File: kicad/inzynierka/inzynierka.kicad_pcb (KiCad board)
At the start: 2 copper layers, 170 x 175 mm, 36 parts

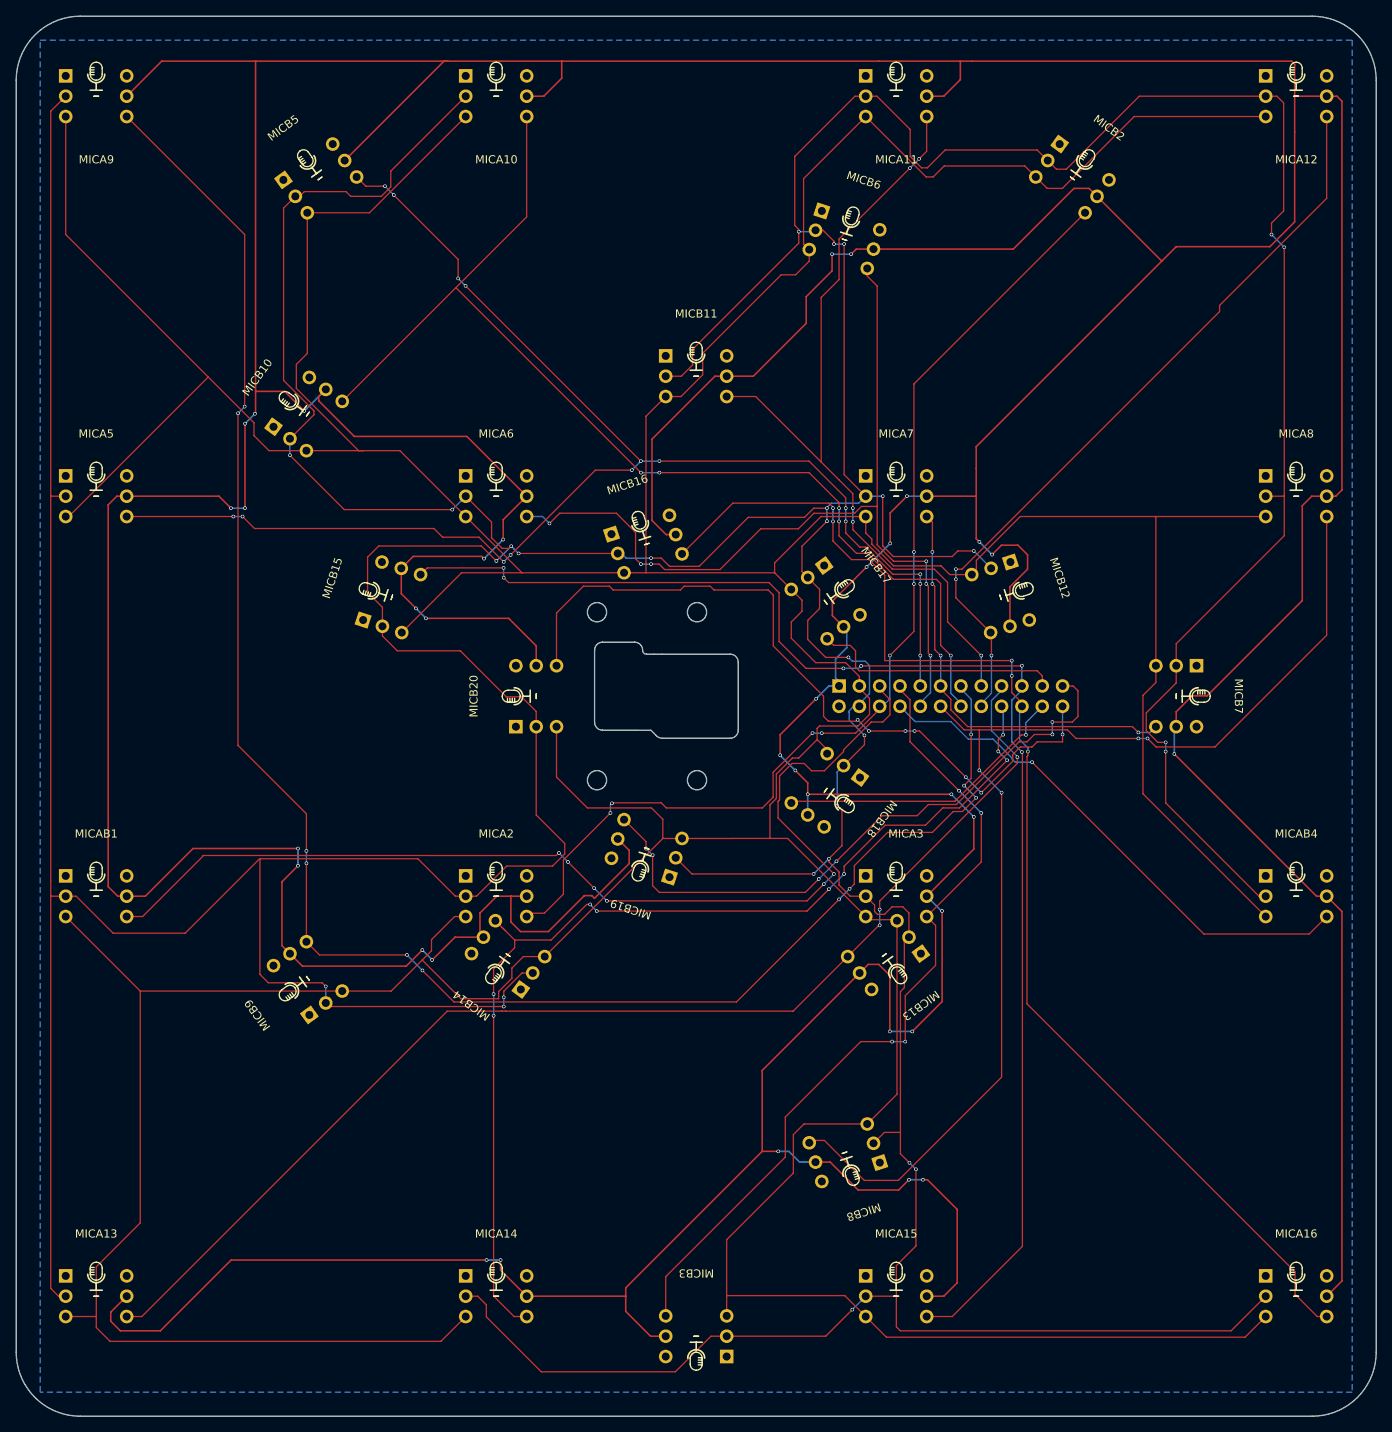
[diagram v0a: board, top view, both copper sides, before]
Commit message: Dodanie dziur montażowych
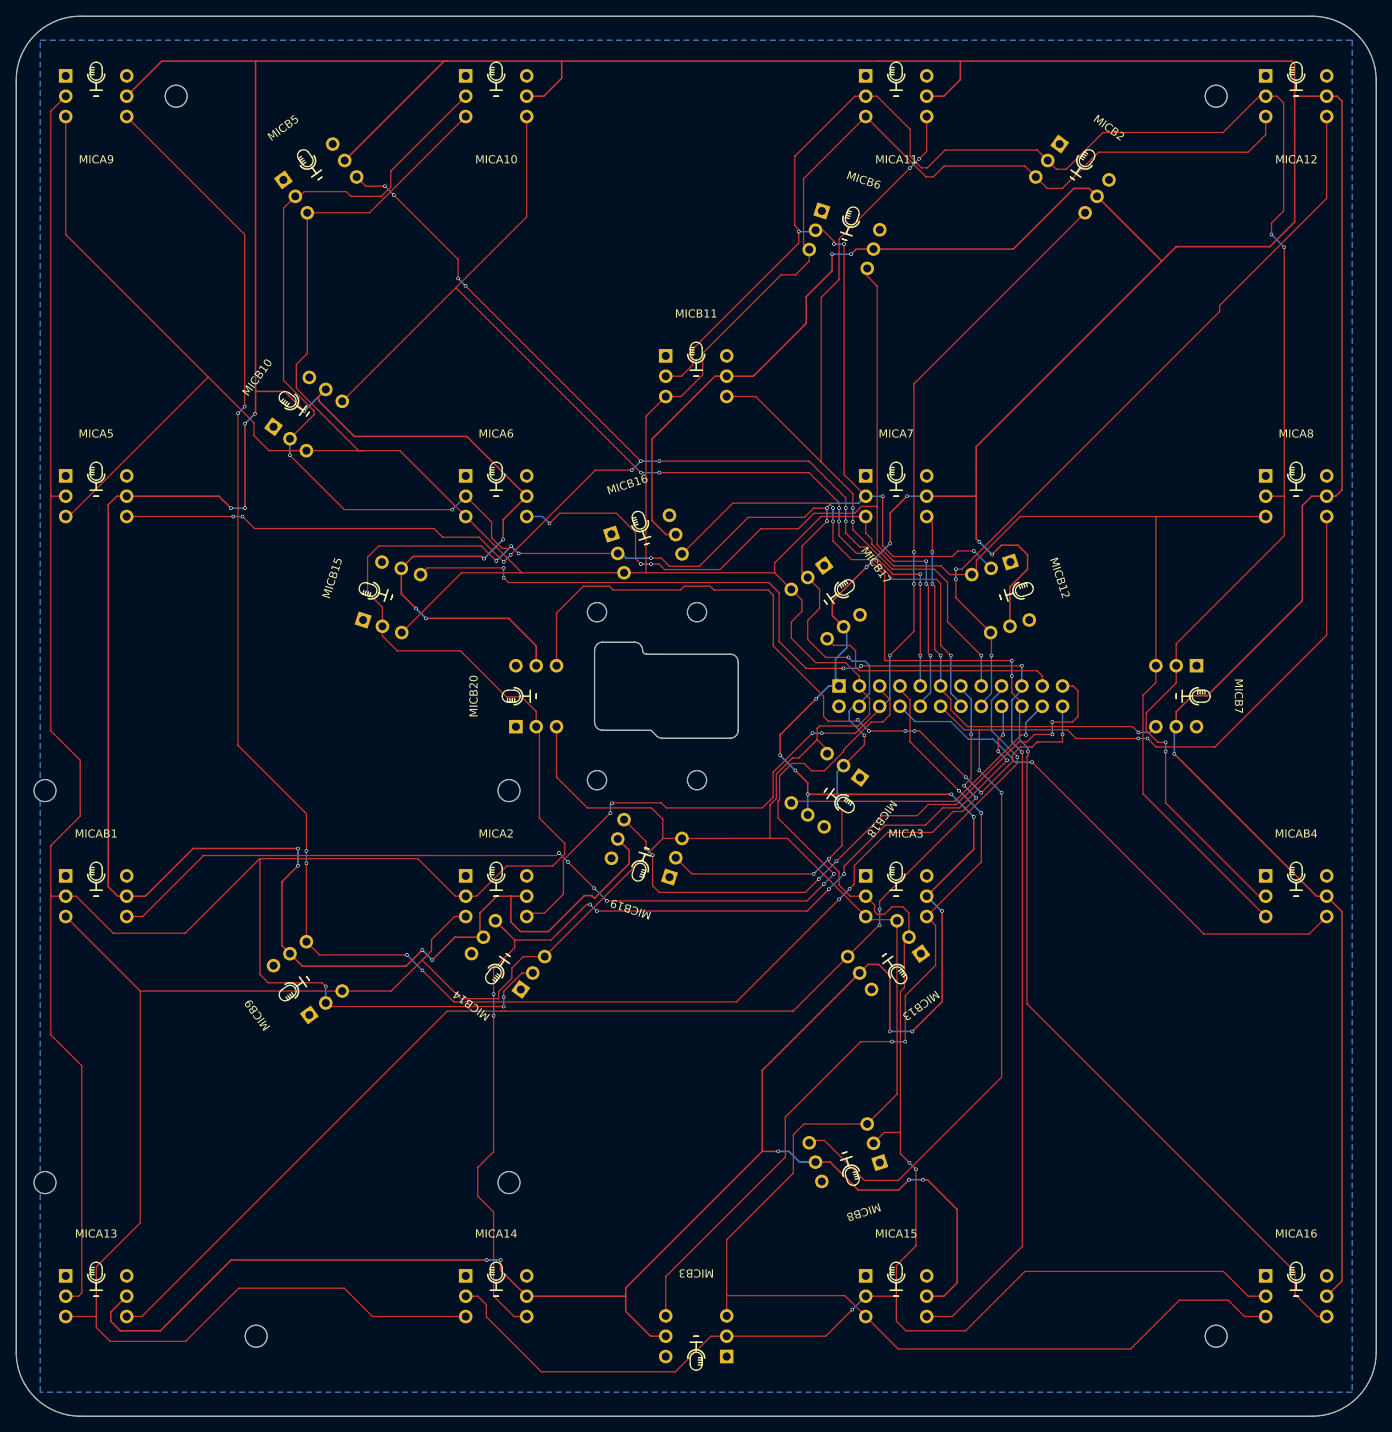
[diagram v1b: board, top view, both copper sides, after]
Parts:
- added ?: , , F.Cu at (46.5, 180.0)
- added ?: , , F.Cu at (166.5, 180.0)
- added ?: , , F.Cu at (166.5, 25.0)
- added ?: , , F.Cu at (36.5, 25.0)
- added REF**: RPI 3B, Moje:RPI 3B, B.Cu at (39.1, 136.3)
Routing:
- net CLK2: track 1057.2 -> 1064.5 mm
- net CLK1: track 923.9 -> 931.1 mm
- net D14: track 134.4 -> 136.1 mm

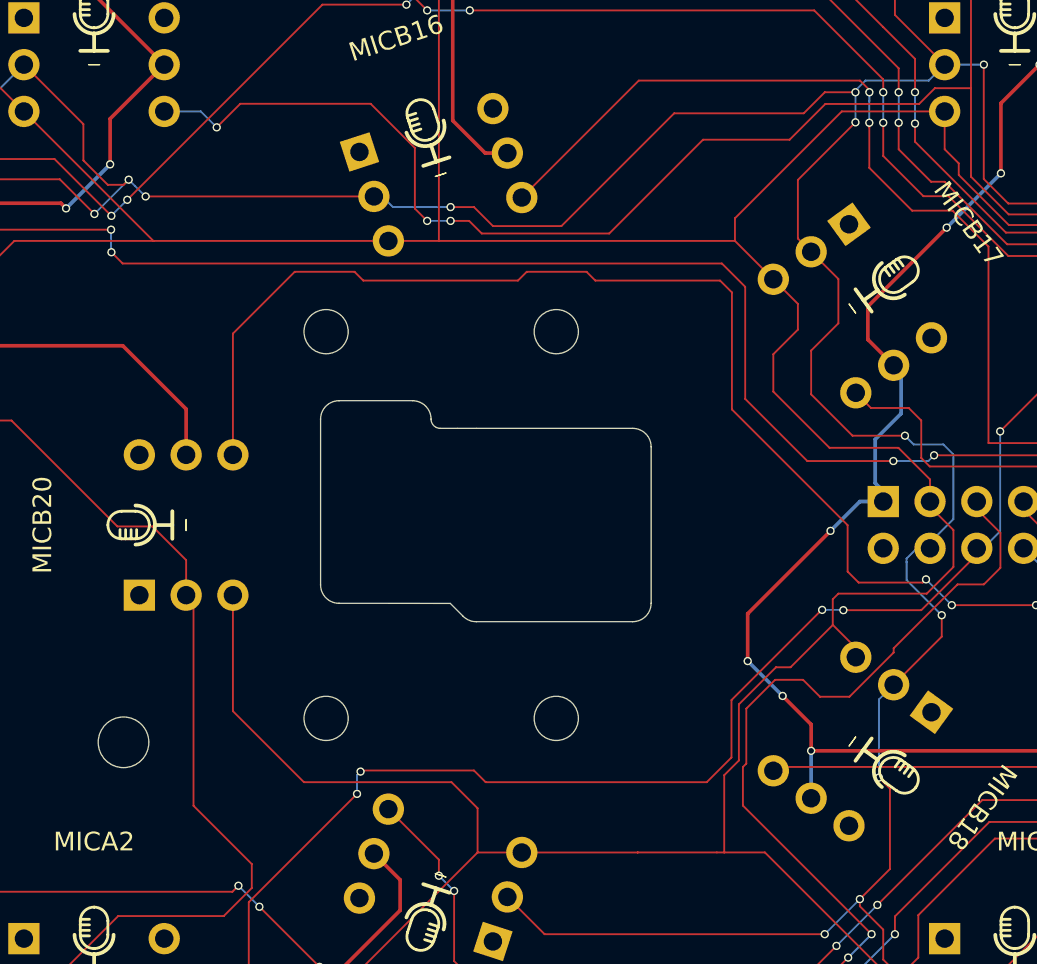
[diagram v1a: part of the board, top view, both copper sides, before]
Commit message: Poprawienie footprintu i odwrócenie kamery
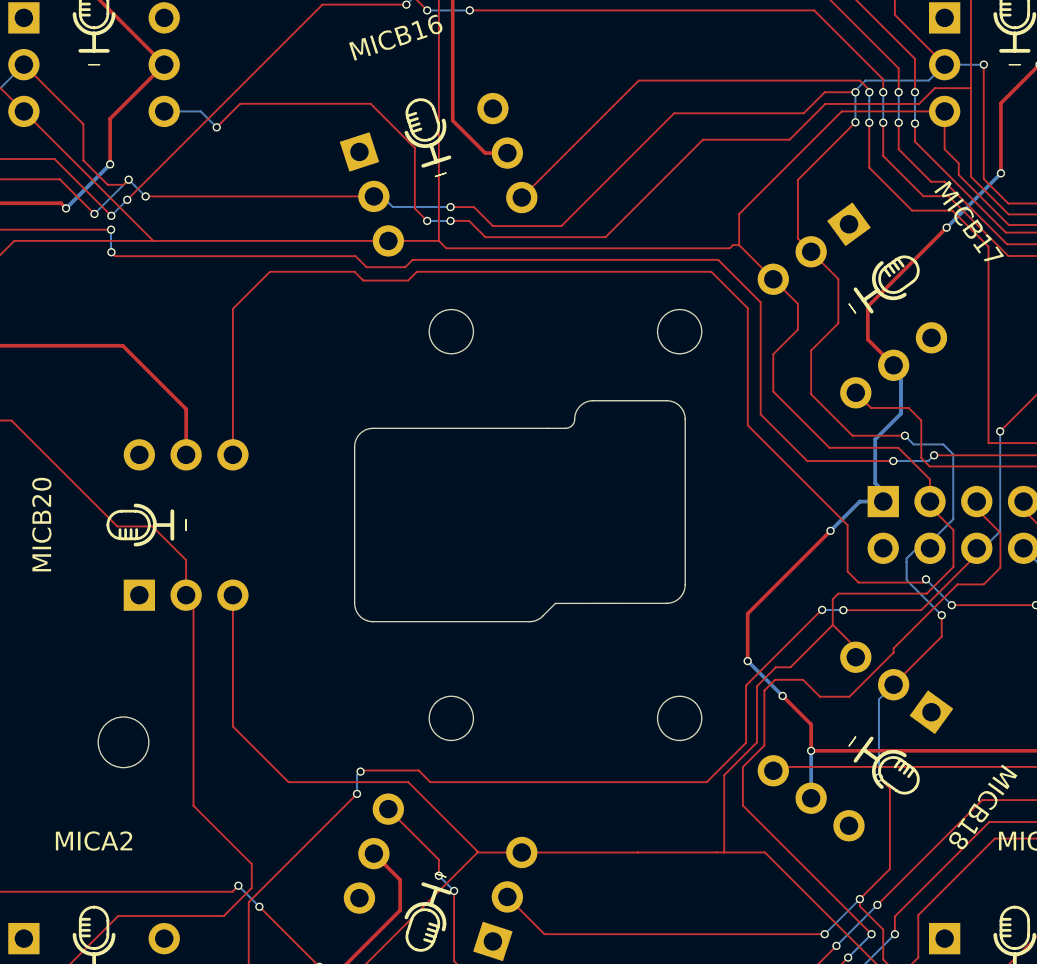
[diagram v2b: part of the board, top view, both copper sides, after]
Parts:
- moved REF** 5.60 mm to (95.9, 100.0), turned to -90 degrees
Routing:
- net D20: track 95.2 -> 96.0 mm
- net CLK1: track 931.1 -> 930.5 mm

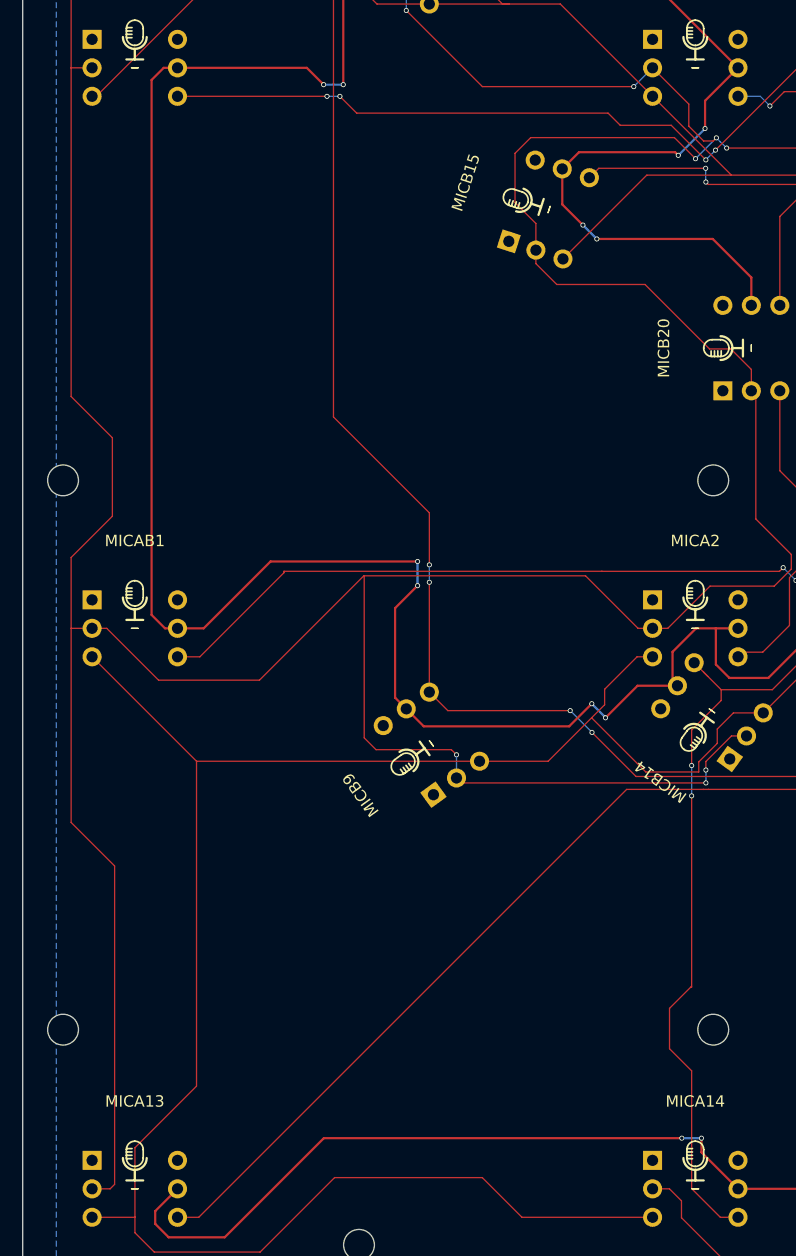
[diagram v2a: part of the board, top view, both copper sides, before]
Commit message: Przesunięto dziury montażowe dla RPI 3
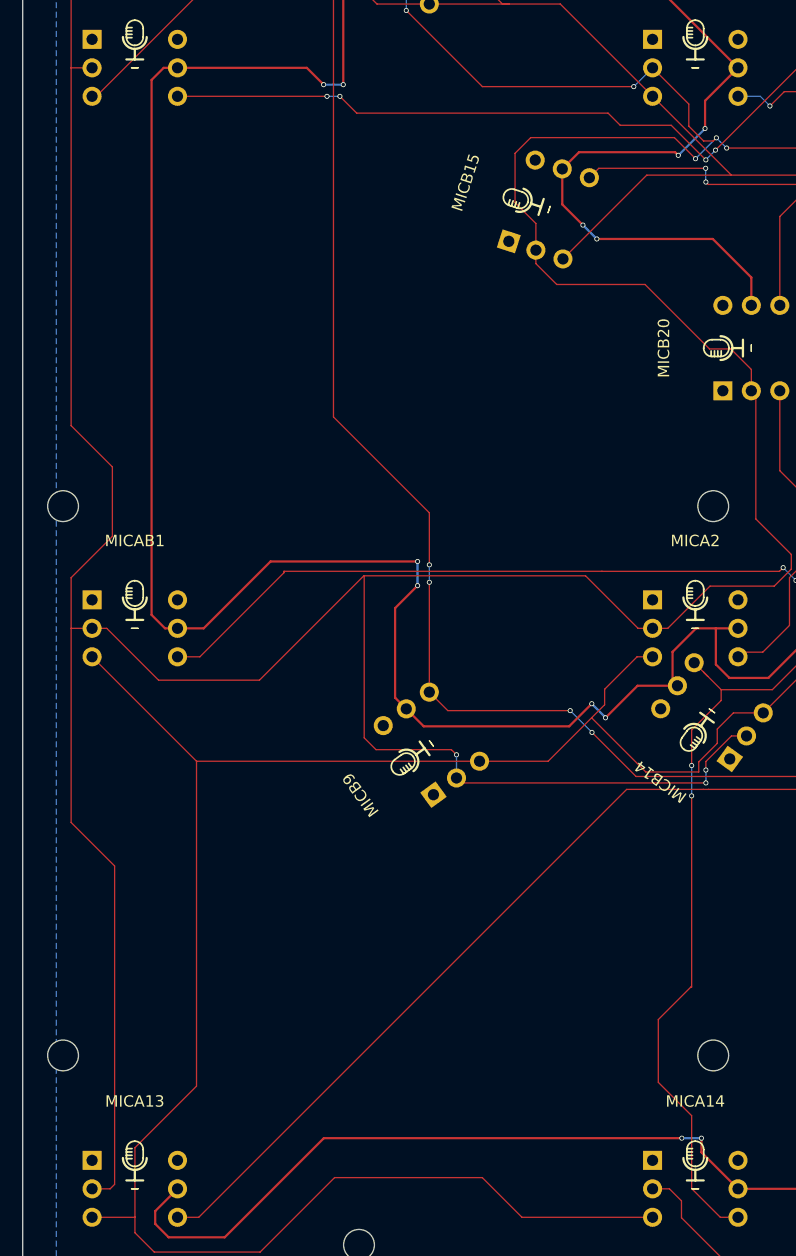
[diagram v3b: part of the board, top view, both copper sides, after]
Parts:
- moved REF** 2.30 mm to (39.1, 138.6)
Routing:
- net D14: track 136.1 -> 136.9 mm

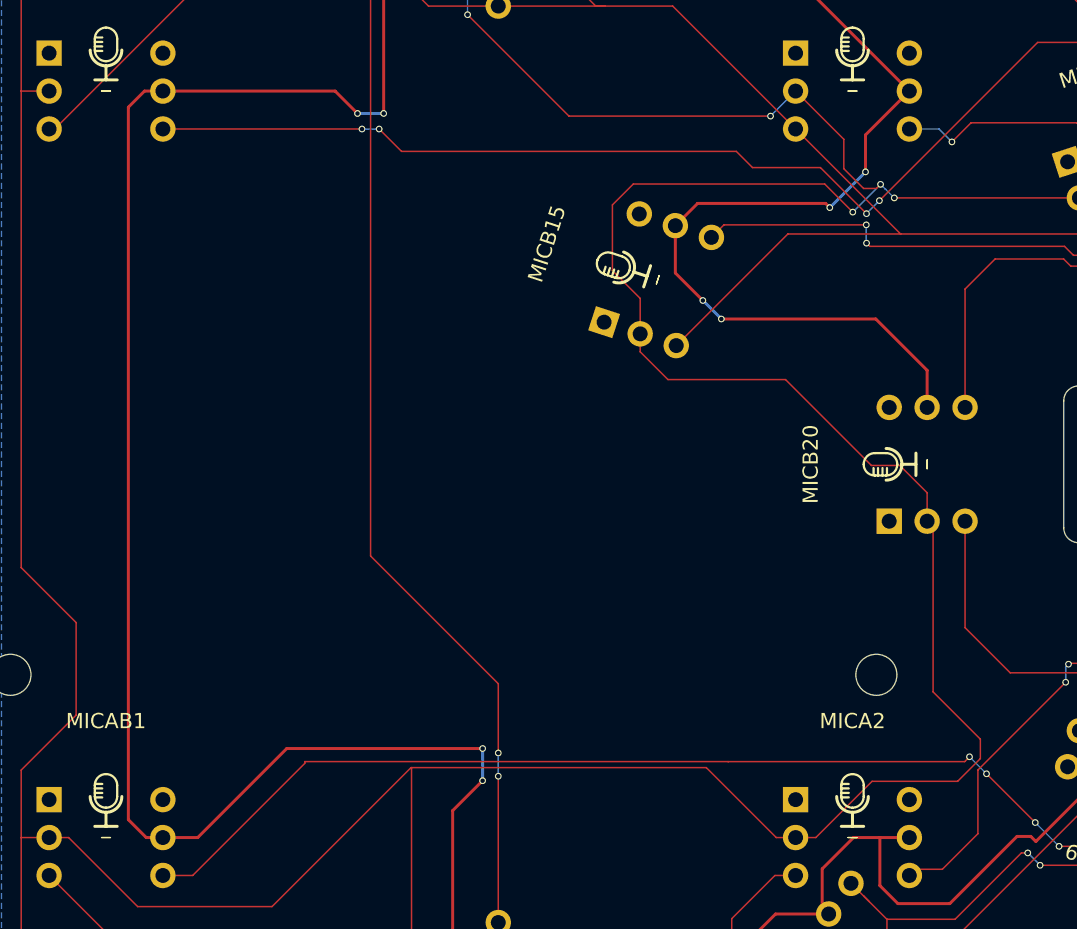
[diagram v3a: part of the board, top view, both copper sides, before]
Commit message: Rozpoczęcie dodawania opisów z tyłu płytki
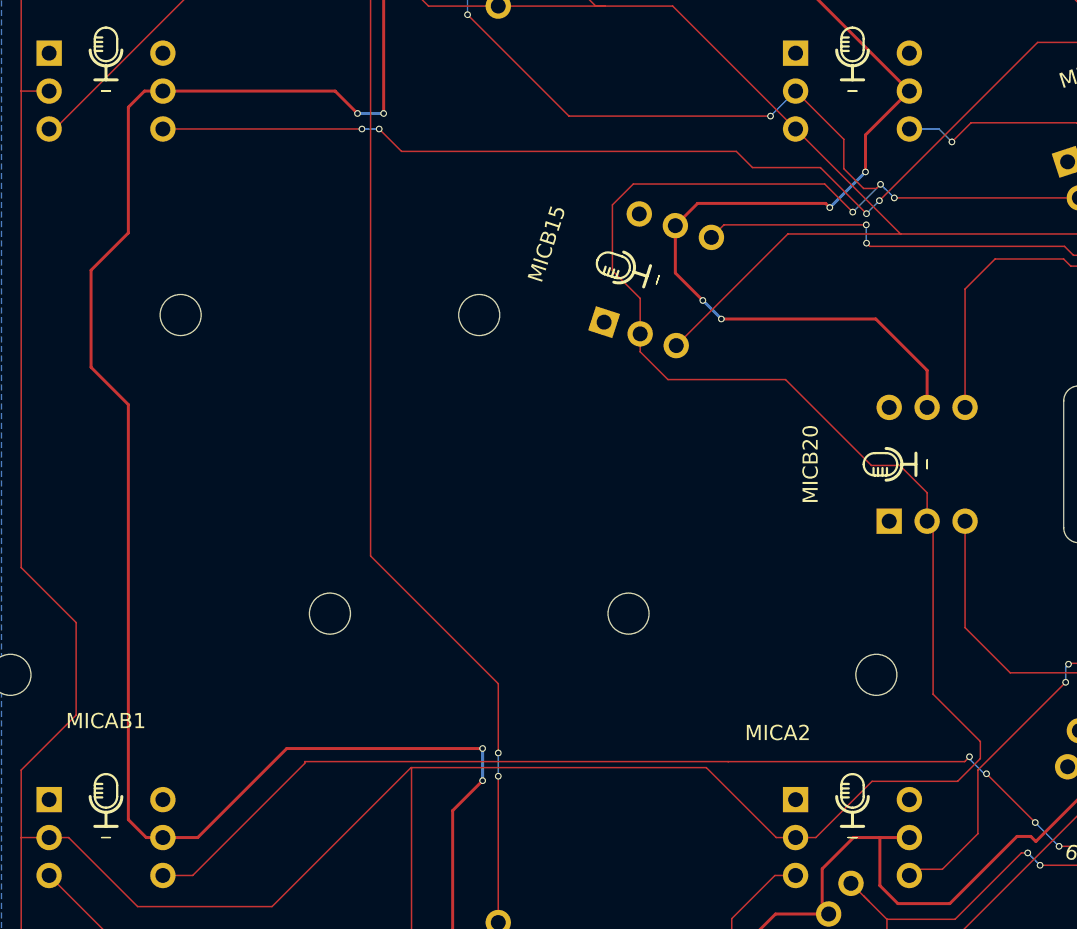
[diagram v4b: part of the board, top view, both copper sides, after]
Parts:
- added ?: , , F.Cu at (61.5, 110.0)
- added ?: , , F.Cu at (31.5, 90.0)
- added ?: , , F.Cu at (41.5, 110.0)
- added ?: , , F.Cu at (51.5, 90.0)
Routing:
- net +3.3V: track 1178.5 -> 1180.6 mm
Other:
- board text added: "X"
- board text added: "Y"
